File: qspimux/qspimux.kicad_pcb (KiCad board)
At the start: 2 copper layers, 24.8 x 13.8 mm, 16 parts, among them J101 Conn_02x05_Odd_Even, J102 Conn_02x04_Odd_Even, J103 Conn_02x04_Odd_Even, U101 TS3A27518ERTWR, U102 MAX40200AUK, U103 MAX40200AUK

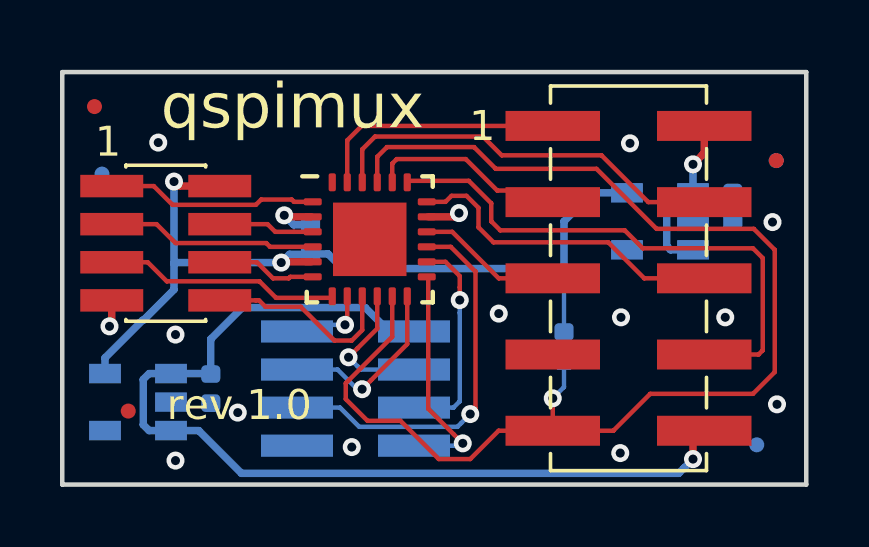
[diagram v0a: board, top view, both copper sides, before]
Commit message: qspimux: update project to use newly included symbols/footprints
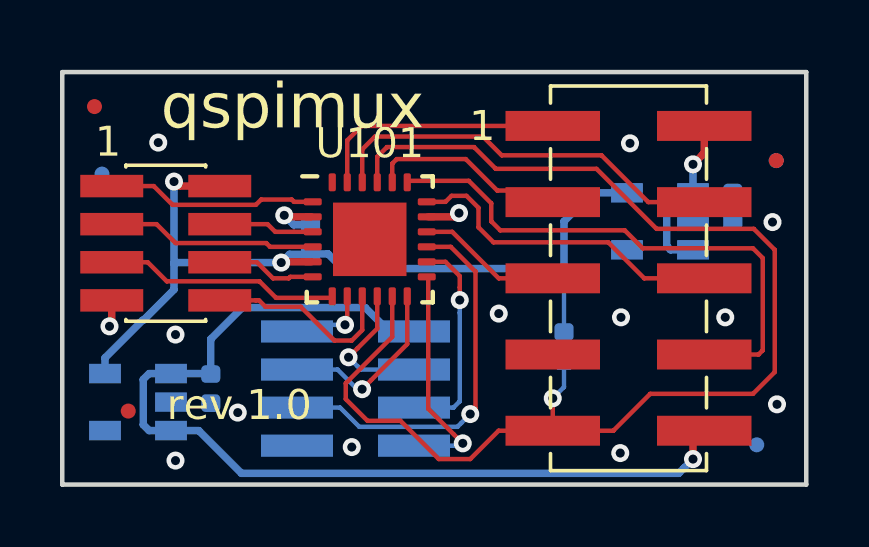
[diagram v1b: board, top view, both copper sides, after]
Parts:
- U101: footprint Package_DFN_QFN:QFN-24_1EP_3.9x3.9mm_Pitch0.5mm -> qspimux-footprints:QFN-24_1EP_3.9x3.9mm_Pitch0.5mm

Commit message: qspimux: fix remaining net name bug
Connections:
- net /IO0_DO_BOARD renamed /IO1_DO_BOARD
- net /IO0_DO_FLASH renamed /IO1_DO_FLASH
